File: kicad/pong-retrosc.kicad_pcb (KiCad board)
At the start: 2 copper layers, 80 x 66 mm, 22 parts, among them J1 RCA video (na placa), J4 chave A/B (painel), J5 pot P1 (painel), J6 pot P2 (painel), J7 START (painel), J8 RCA audio L (na placa), J9 RCA audio R (na placa), U1 RaspberryPi_Pico, U2 PAM8403 HW-012

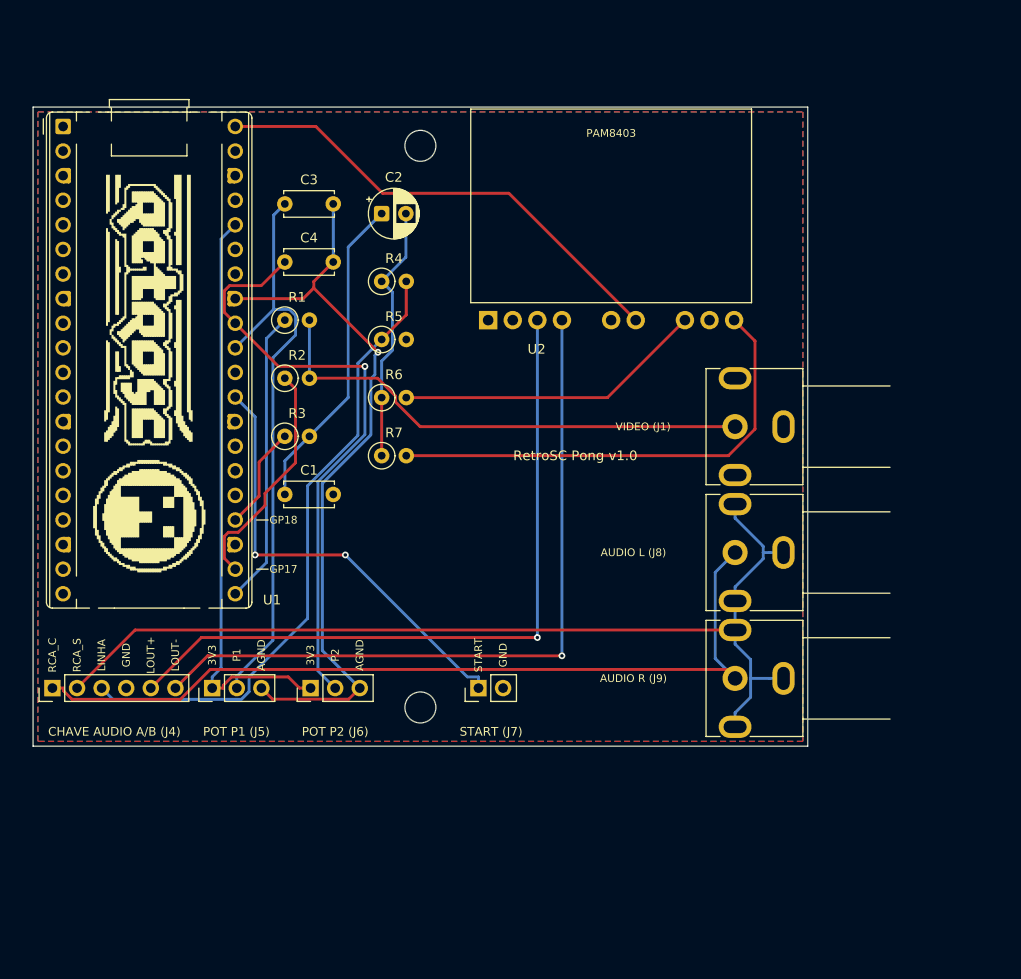
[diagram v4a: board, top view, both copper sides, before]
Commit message: kicad: afasta os headers na borda de baixo
J4 e J5 ficavam a 0,26 mm um do outro e as descricoes ("CHAVE AUDIO A/B
(J4)" / "POT P1 (J5)") corriam juntas.

Nao dava para so espacar: J4+J5+J6 ocupavam 35,0 mm dos 36,4 disponiveis
ate a area de exclusao do furo, e o par J5/J6 e indivisivel (a vaga entre
eles existe para um unico conector femea 1x7 servir os dois). Entao quem
mudou de lugar foi o START, que e independente:

  antes:  J4  J5 J6 ......... J7
  agora:  J4 ..... J7 ..... J5 J6      (o par a direita do furo)

Folgas: 7,8 mm entre J4 e J7 e 14,9 mm entre J7 e J5. O rotulo do J9
subiu, que o par passou a ocupar a faixa onde ele estava.

DRC 0 erros nas duas placas; serigrafia sem sobreposicao nem silk sobre
cobre. Gerbers, ZIPs, renders e desenho de encaixe regenerados.

Co-Authored-By: Claude Opus 5 <noreply@anthropic.com>
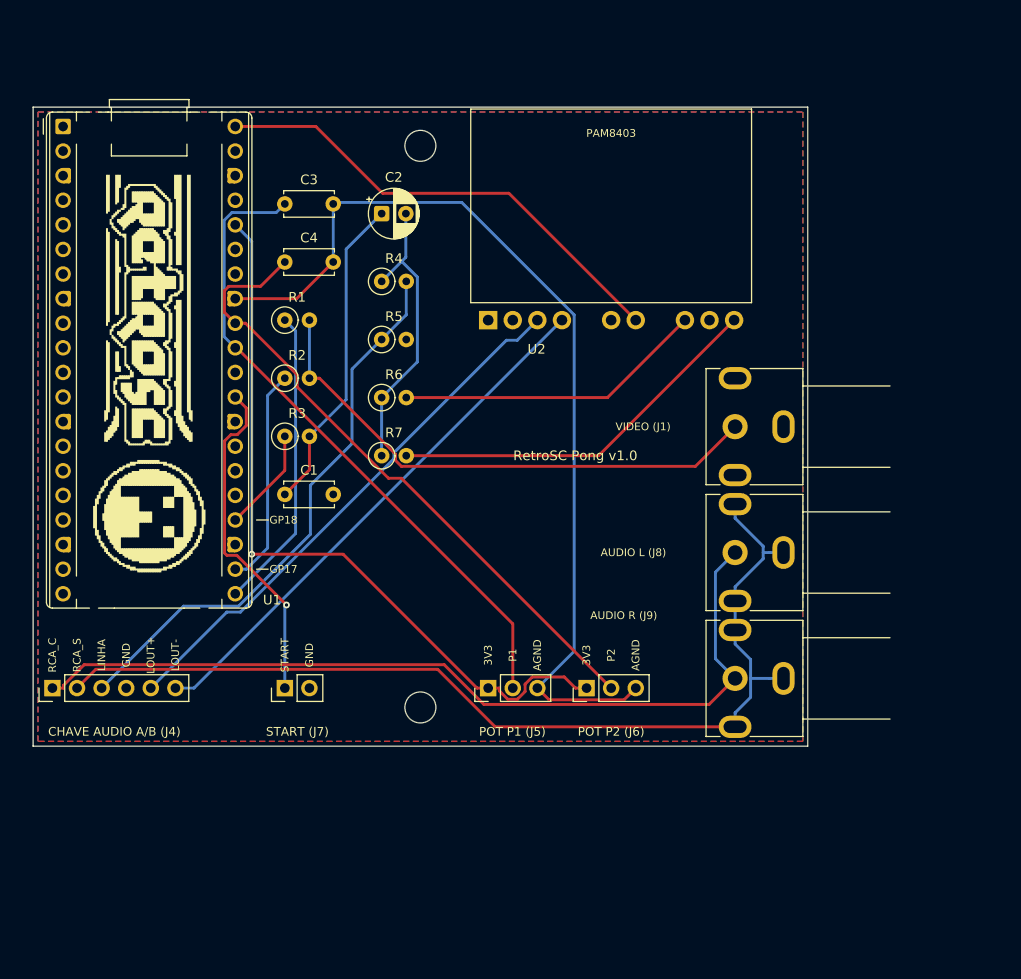
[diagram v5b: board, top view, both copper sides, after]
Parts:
- moved J5 28.5 mm to (67.0, 80.0)
- moved J6 28.5 mm to (77.2, 80.0)
- moved J7 20.0 mm to (46.0, 80.0)
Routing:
- net AGND: track 77.2 -> 98.7 mm, vias 1 -> 0
- net LOUT_N: track 76.0 -> 55.7 mm, vias 1 -> 0
- net LOUT_P: track 74.9 -> 56.0 mm, vias 1 -> 0
- net +3V3: track 60.1 -> 77.6 mm, vias 0 -> 1
- net START: track 46.6 -> 35.2 mm, vias 2 -> 1
- net AMP_R: track 49.3 -> 39.7 mm
- net POT1: track 60.5 -> 67.7 mm
- net LINHA: track 65.1 -> 58.4 mm
- net POT2: track 62.5 -> 66.4 mm, vias 1 -> 0
- net COMPOSITE: track 52.4 -> 55.8 mm
- net AUD_C: track 27.0 -> 30.3 mm
- net VIDEO: track 24.3 -> 22.5 mm
- net RCA_C: track 87.5 -> 89.2 mm
- net SYNC: track 30.4 -> 31.3 mm
- net RCA_S: track 102.7 -> 103.4 mm

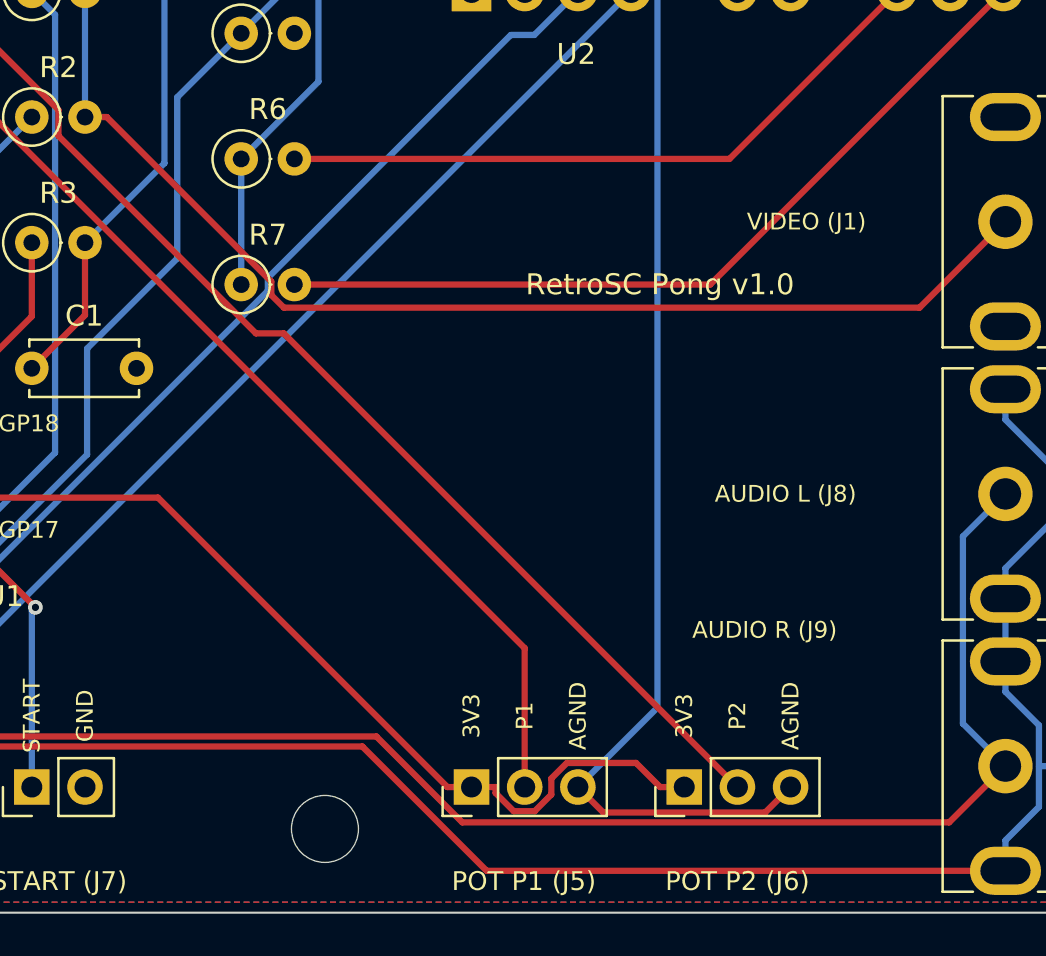
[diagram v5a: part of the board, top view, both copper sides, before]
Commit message: kicad: rotulos dos RCAs na vertical e assinatura no meio da placa
- VIDEO/AUDIO L/AUDIO R passam a ser verticais (rot 90), encostados na
  lateral de cada jack: acompanham a altura do conector, ficam sem duvida
  de qual e qual e nao disputam espaco com a faixa dos headers. O
  "AUDIO R" em especial estava solto, longe do seu jack.
- assinatura na area vazia do centro: "RetroSC Pong v1.0" em 1,6 mm e
  "LRRosa 2026" em 1,1 mm logo abaixo.

DRC 0 erros nas duas placas, sem silk sobre cobre nem sobreposicao.
Gerbers, ZIPs, renders e desenho de encaixe regenerados.

Co-Authored-By: Claude Opus 5 <noreply@anthropic.com>
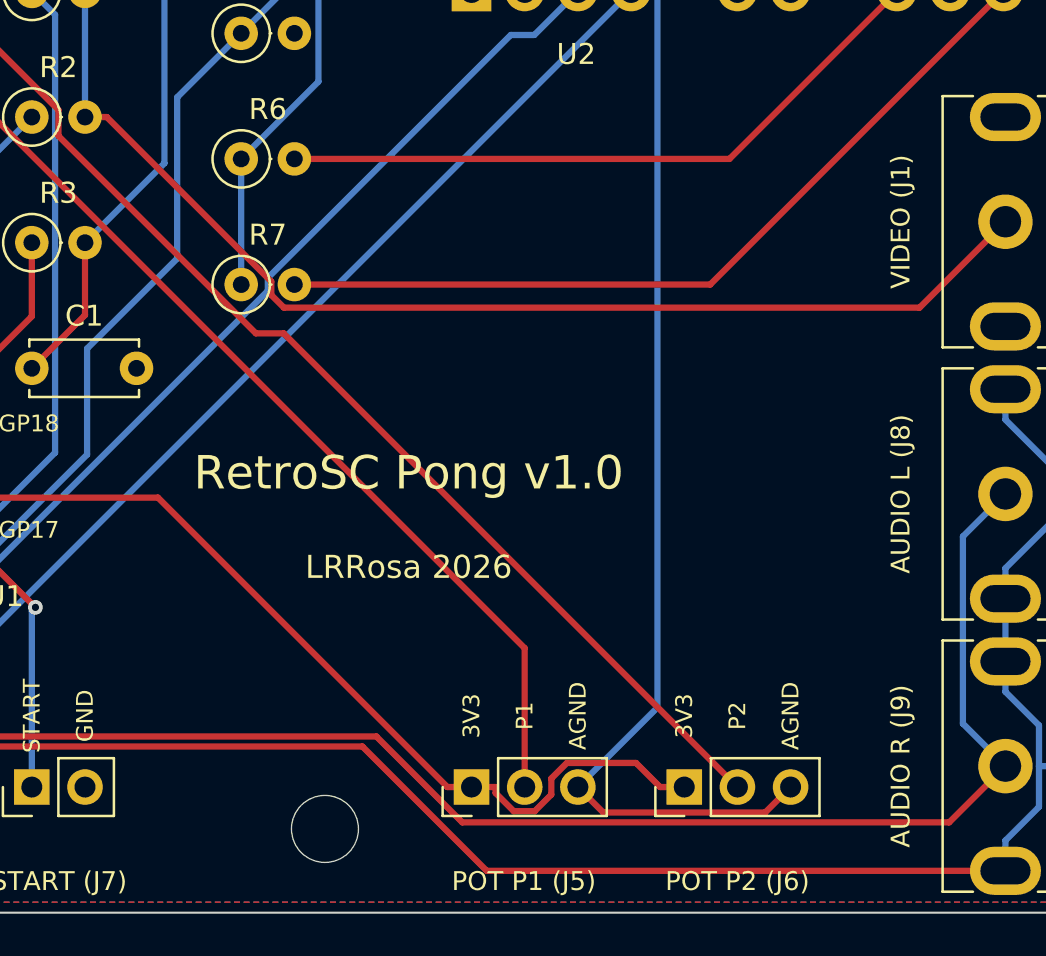
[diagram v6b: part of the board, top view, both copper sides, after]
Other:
- board text added: "LRRosa 2026"
